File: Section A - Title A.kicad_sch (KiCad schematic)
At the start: 41 parts, among them U1 AD7190WBRUZ, Y1 ABC2-4.9152MHZ-4-T

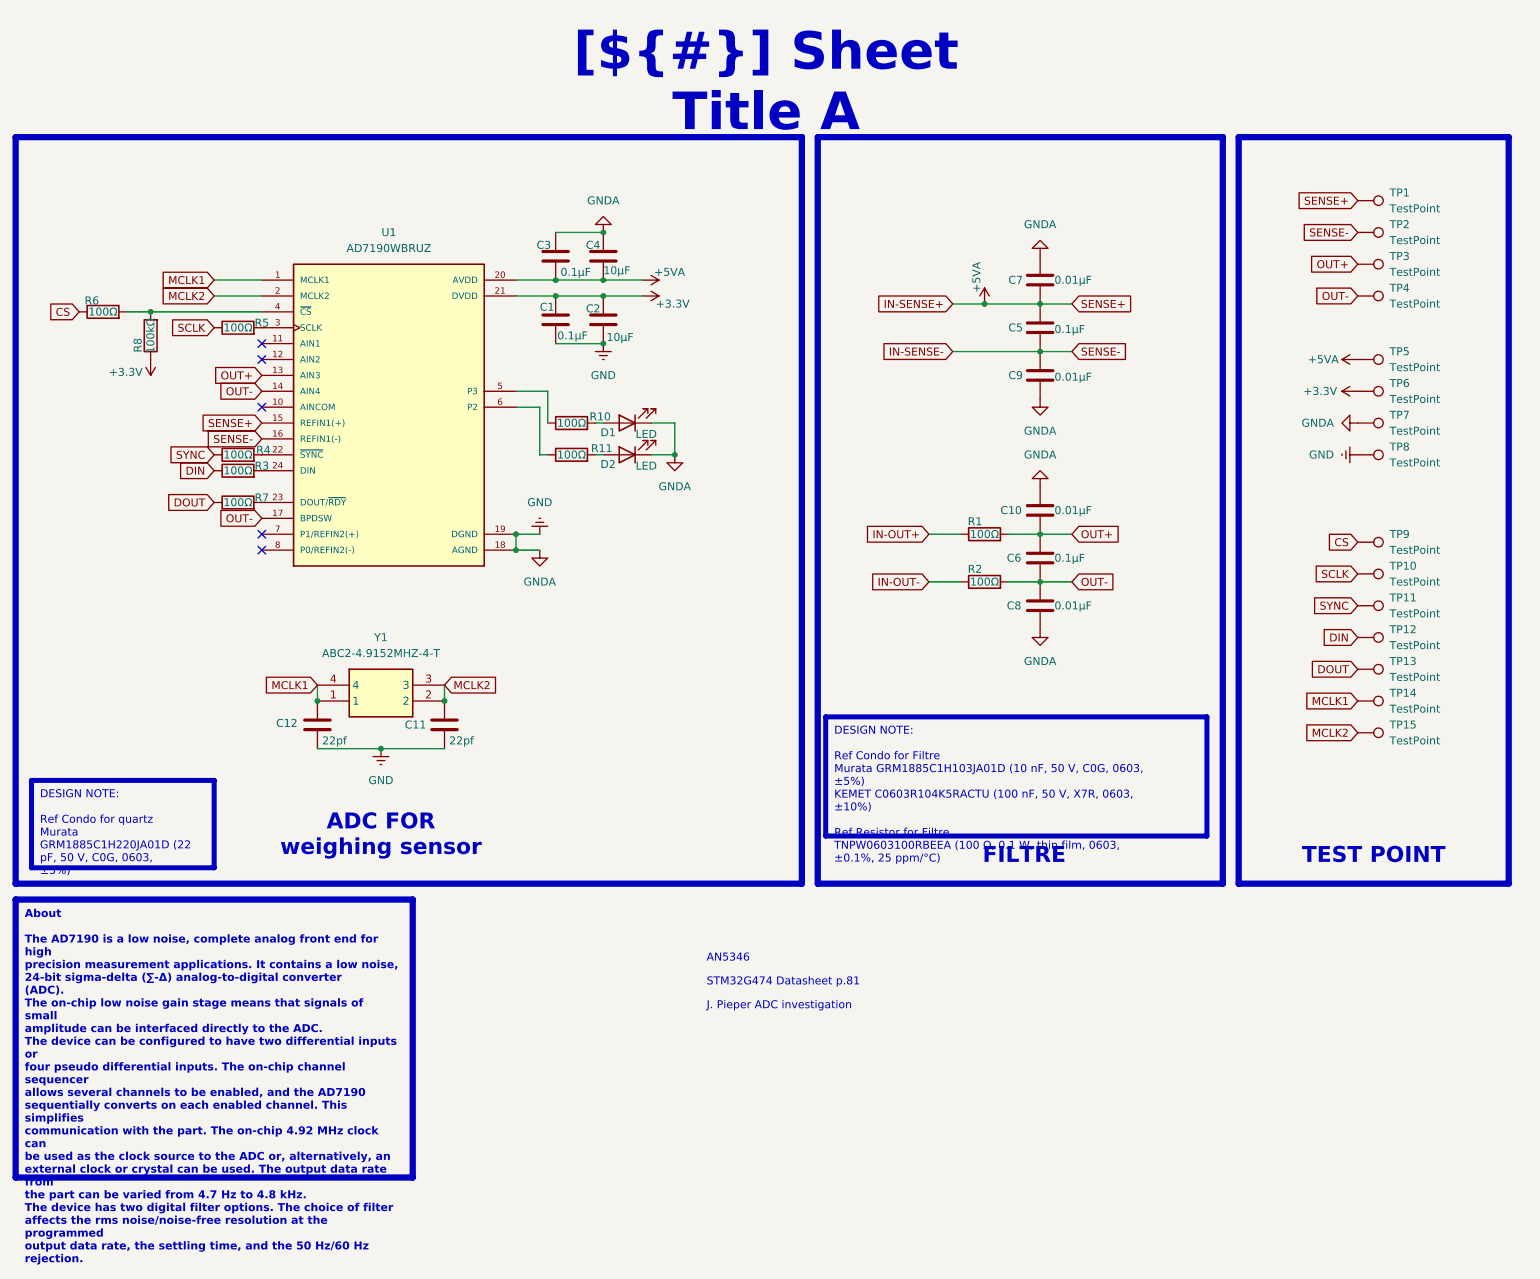
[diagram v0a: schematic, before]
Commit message: [FINISH LT3042 and ad TPS6108]
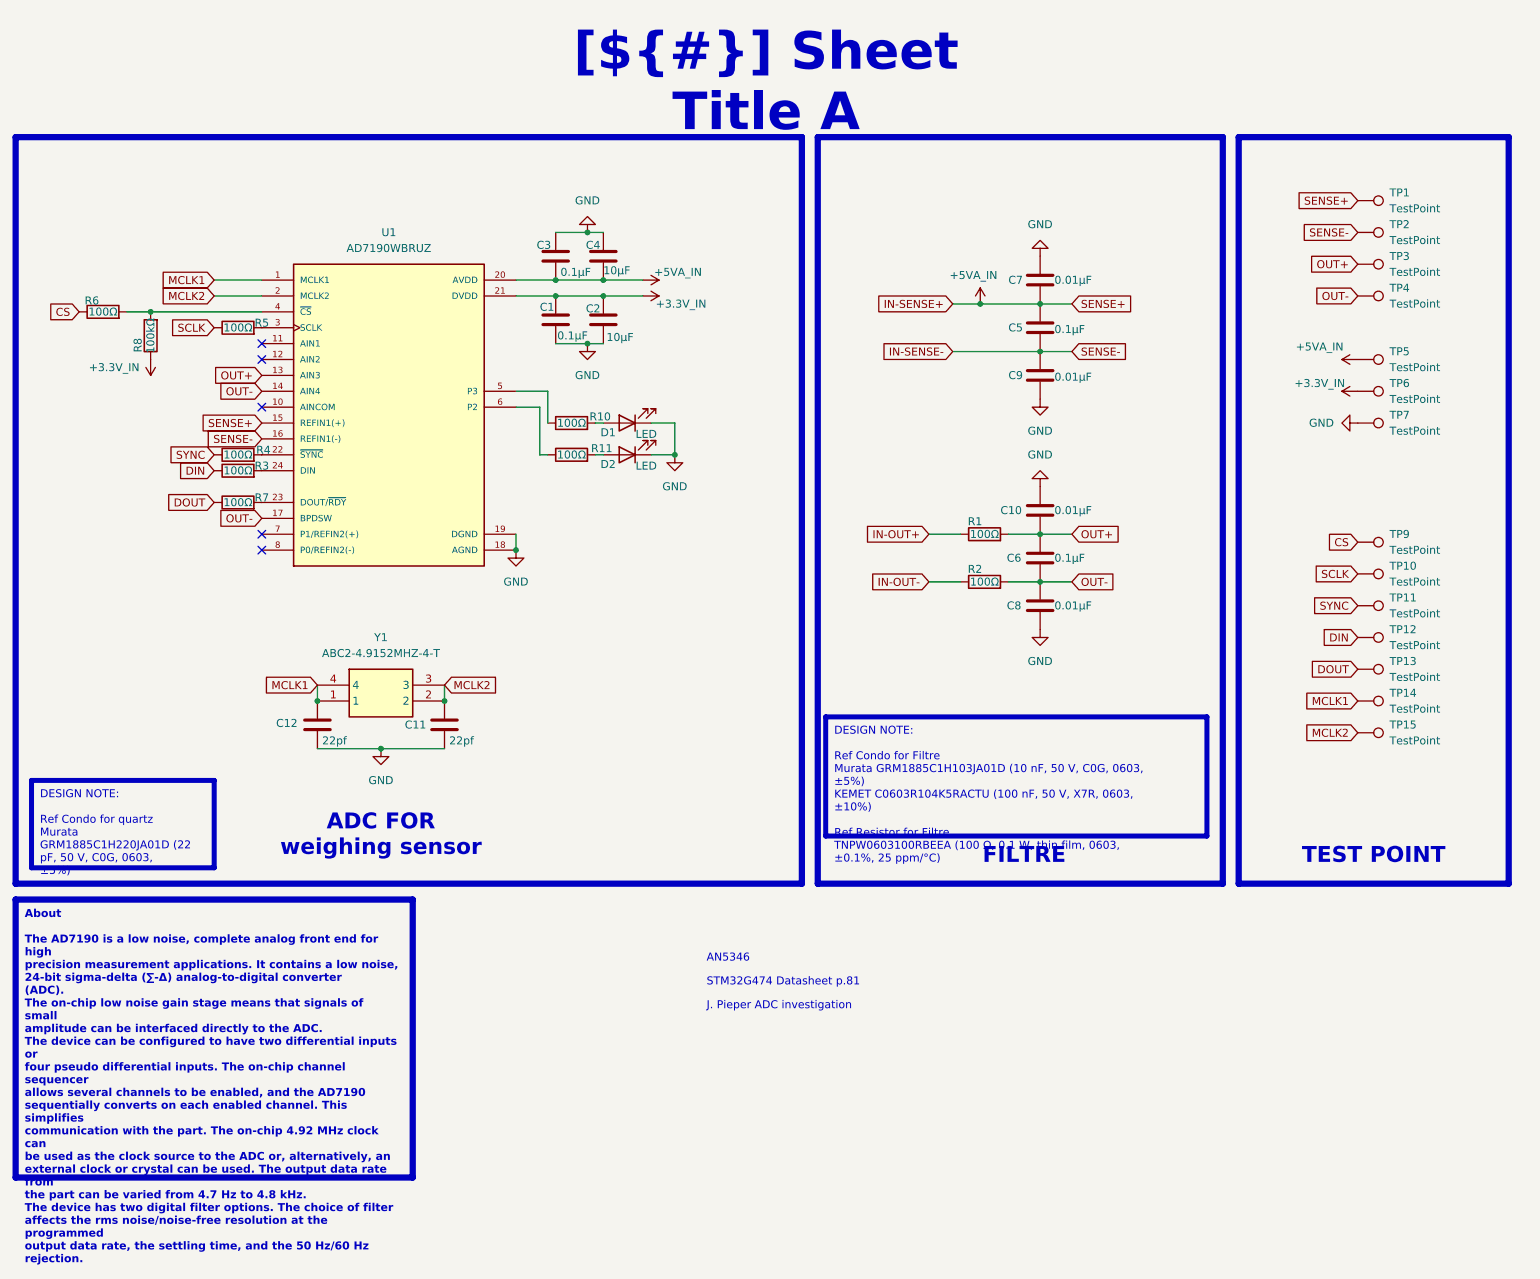
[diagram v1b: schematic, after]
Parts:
- removed TP8: TestPoint, TestPoint:TestPoint_Pad_D2.0mm, symbol Connector:TestPoint
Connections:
- net +3.3V renamed +3.3V_IN
- net +5VA renamed +5VA_IN

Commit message: [Finish schématiq]
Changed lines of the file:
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@@
 		)
 	)
-	(text_box "[${#}] ${TITLE}"
+	(text_box "[${#}] AD7910_Weight_sensor"
 		(exclude_from_sim no)
-		(at 115.57 15.24 0)
-		(size 72.39 12.7)
+		(at 92.71 15.24 0)
+		(size 113.03 12.7)
 		(margins 4.4999 4.4999 4.4999 4.4999)
 		(stroke
 			(width -0.0001)
-			(type default)
+			(type solid)
 		)
 		(fill

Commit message: [PCB fini]
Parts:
- removed TP10, TP11, TP12, TP13, TP9: TestPoint, TestPoint:TestPoint_Pad_D2.0mm, symbol Connector:TestPoint
- Y1: footprint ABC210000MHZ4 -> ABC2-4.9152MHZ-4-T:ABC210000MHZ4
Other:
- moved on the sheet: TP14, TP15

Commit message: [PCB 4 layer]
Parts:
- removed D1: LED, LED_SMD:LED_0603_1608Metric, symbol Device:LED
- removed R3, R4, R5, R7: 100Ω, Resistor_SMD:R_0603_1608Metric, symbol Device:R
- removed Y1: ABC2-4.9152MHZ-4-T, ABC2-4.9152MHZ-4-T:ABC210000MHZ4, symbol ABC2-4_9152MHZ-4-T:ABC2-4.9152MHZ-4-T
- added C23, C26: 0.1µF, Capacitor_SMD:C_0603_1608Metric, symbol Device:C
- added C24, C25: 18pf, Capacitor_SMD:C_0603_1608Metric, symbol Device:C
- added Q1: SI2303CDS-T1-GE3, Package_TO_SOT_SMD:SOT-23-3, symbol Transistor_FET:CSD25480F3
- added RN1: RP_100Ω, Resistor_SMD:R_Array_Concave_4x0603, symbol Device:R_Pack04
- added Y2: CSTCR4M91G53-R0, CSTCR4M91G53-R0:OSC_CSTCR4M91G53-R0, symbol CSTCR4M91G53-R0:CSTCR4M91G53-R0
- C11: value 22pf -> 0.1µF
- C12: value 22pf -> 10µF
- D2: value LED -> RED
- R10: value 100Ω -> 1kΩ
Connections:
- net DIN: now also RN1.5 (R4.2)
- net DOUT: now also RN1.6 (R3.2)
- net GND: now also U1.9 (NC), C23.2, C24.2, C25.2, C26.2, Y2.2
- net MCLK1: now also C25.1, Y2.1; no longer C12.1
- net MCLK2: now also C24.1, Y2.3; no longer C11.1
- net SCLK: now also RN1.8 (R1.2)
- net SYNC: now also RN1.7 (R2.2)
- net at U1.3 (SCLK): now also RN1.1 (R1.1)
- net P3: now reaches R10.1, U1.5 (P3)
- net at R10.2: now also Q1.1 (G)
- net at U1.24 (DIN): now also RN1.4 (R4.1)
- net at U1.22 (~{SYNC}): now also RN1.2 (R2.1)
- net at U1.23 (DOUT/~{RDY}): now also RN1.3 (R3.1)
- net +3.3V_IN renamed +3.3V
- net +5VA_IN renamed +5VA
- net +5VA: now also C12.1, C26.1, Q1.2 (S); no longer C5.1, C7.2, TP1.1, U1.15 (REFIN1(+))
- net IN-SENSE- renamed SENSE-
- new net SENSE+: C11.1, C23.1, C5.1, C7.2, Q1.3 (D), TP1.1, U1.15 (REFIN1(+))
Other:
- moved on the sheet: C1, C2, C3, C4, D2, R1, R11, R2, R6, R8, TP1, TP14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

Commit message: [PCB V1]
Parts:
- removed TP14, TP15: TestPoint, TestPoint:TestPoint_Pad_D2.0mm, symbol Connector:TestPoint
- added TP8, TP9: TestPoint, TestPoint:TestPoint_Pad_D1.5mm, symbol Connector:TestPoint
- TP1, TP2, TP3, TP4, TP5, TP6, TP7: footprint TestPoint:TestPoint_Pad_D2.0mm -> TestPoint:TestPoint_Pad_D1.5mm
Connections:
- net +3.3V: now also TP4.1; no longer TP6.1
- net GND: now also TP3.1; no longer TP7.1
- net MCLK1: now also TP2.1
- net MCLK2: now also TP1.1
- net OUT+: now also TP7.1; no longer TP3.1
- net OUT-: now also TP6.1; no longer TP4.1
- net SENSE+: now also TP9.1; no longer TP1.1
- net SENSE-: now also TP8.1; no longer TP2.1

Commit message: [PCB V2]
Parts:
- added TP18: TestPoint, TestPoint:TestPoint_Pad_D1.5mm, symbol Connector:TestPoint
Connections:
- net P3: now also TP18.1
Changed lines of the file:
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@@
+		)
+	)
+	(global_label "P3"
+		(shape input)
+		(at 250.19 88.9 180)
+		(fields_autoplaced yes)
+		(effects
+			(font
+				(size 1.27 1.27)
+			)
+			(justify right)
+		)
+		(property "Intersheetrefs" "${INTERSHEET_REFS}"
+			(at 244.7253 88.9 0)
+			(effects
+				(font
+					(size 1.27 1.27)
+				)
+				(justify right)
+				(hide yes)
+			)
 		)
 	)
@@
 					(unit 1)
 				)
+			)
+		)
+	)
+	(symbol
+		(lib_id "Connector:TestPoint")
+		(at 250.19 88.9 270)
+		(unit 1)
+		(exclude_from_sim no)
+		(in_bom yes)
+		(on_board yes)
+		(dnp no)
+		(fields_autoplaced yes)
+		(property "Reference" "TP18"
+			(at 255.27 87.6299 90)
+			(effects
+				(font
+					(size 1.27 1.27)
+				)
+				(justify left)
+				(hide yes)
+			)
+		)
+		(property "Value" "TestPoint"
+			(at 255.27 90.1699 90)
+			(effects
+				(font
+					(size 1.27 1.27)
+				)
+				(justify left)
+				(hide yes)
+			)
+		)
+		(property "Footprint" "TestPoint:TestPoint_Pad_D1.5mm"
+			(at 250.19 93.98 0)
+			(effects
+				(font
+					(size 1.27 1.27)
+				)
+				(hide yes)
+			)
+		)
+		(property "Datasheet" "~"
+			(at 250.19 93.98 0)
+			(effects
+				(font
+					(size 1.27 1.27)
+				)
+				(hide yes)
+			)
+		)
+		(property "Description" "test point"
+			(at 250.19 88.9 0)
+			(effects
+				(font
+					(size 1.27 1.27)
+				)
+				(hide yes)
+			)
+		)
+		(pin "1"
+		)
+		(instances
+			(project "Cellule_de_force_V2"
+				(path "/f9e05184-c88b-4a88-ae9c-ab2bdb32be7c/c5103ceb-5325-4a84-a025-9638a412984e/f06537ee-772d-44d3-8c50-e0ba41038c9c"
+					(reference "TP18")
+					(unit 1)
+				)

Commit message: [PCB V3]
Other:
- moved on the sheet: C24, C25, D2, Y2
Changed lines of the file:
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@@
 	)
 	(junction
-		(at 100.33 125.73)
+		(at 99.06 125.73)
 		(diameter 0)
 		(color 0 0 0 0)
@@
 	)
 	(junction
-		(at 113.03 113.03)
+		(at 111.76 113.03)
 		(diameter 0)
 		(color 0 0 0 0)
@@
 	)
 	(junction
-		(at 87.63 113.03)
+		(at 86.36 113.03)
 		(diameter 0)
 		(color 0 0 0 0)
@@
 	(wire
 		(pts
-			(xy 119.38 113.03) (xy 113.03 113.03)
+			(xy 114.3 113.03) (xy 111.76 113.03)
 		)
 		(stroke
@@
 	(wire
 		(pts
-			(xy 113.03 125.73) (xy 100.33 125.73)
+			(xy 111.76 125.73) (xy 99.06 125.73)
 		)
 		(stroke
@@
 	(wire
 		(pts
-			(xy 113.03 120.65) (xy 113.03 125.73)
+			(xy 111.76 120.65) (xy 111.76 125.73)
 		)
 		(stroke
@@
 	(wire
 		(pts
-			(xy 87.63 120.65) (xy 87.63 125.73)
+			(xy 86.36 120.65) (xy 86.36 125.73)
 		)
 		(stroke
@@
 	(wire
 		(pts
-			(xy 130.81 72.39) (xy 133.35 72.39)
+			(xy 130.81 72.39) (xy 132.08 72.39)
 		)
 		(stroke
@@
 	(wire
 		(pts
-			(xy 83.82 113.03) (xy 87.63 113.03)
+			(xy 82.55 113.03) (xy 86.36 113.03)
 		)
 		(stroke
@@
 	(wire
 		(pts
-			(xy 140.97 72.39) (xy 146.05 72.39)
+			(xy 139.7 72.39) (xy 146.05 72.39)
 		)
 		(stroke
@@
 	(wire
 		(pts
-			(xy 87.63 125.73) (xy 100.33 125.73)
+			(xy 86.36 125.73) (xy 99.06 125.73)
 		)
 		(stroke
@@
 	(global_label "MCLK1"
 		(shape input)
-		(at 83.82 113.03 180)
+		(at 82.55 113.03 180)
 		(fields_autoplaced yes)
 		(effects
@@
 		)
 		(property "Intersheetrefs" "${INTERSHEET_REFS}"
-			(at 74.6058 113.03 0)
+			(at 73.3358 113.03 0)
 			(effects
 				(font
@@
 	(global_label "MCLK2"
 		(shape input)
-		(at 119.38 113.03 0)
+		(at 114.3 113.03 0)
 		(fields_autoplaced yes)
 		(effects
@@
 		)
 		(property "Intersheetrefs" "${INTERSHEET_REFS}"
-			(at 128.5942 113.03 0)
+			(at 123.5142 113.03 0)
 			(effects
 				(font
@@
 	(symbol
 		(lib_id "Device:C")
-		(at 113.03 116.84 0)
+		(at 111.76 116.84 0)
 		(unit 1)
 		(exclude_from_sim no)
@@
 		(dnp no)
 		(property "Reference" "C24"
-			(at 113.284 118.872 0)
+			(at 112.014 118.872 0)
 			(effects
 				(font
@@
 		)
 		(property "Value" "18pf"
-			(at 115.57 116.84 0)
+			(at 114.3 116.84 0)
 			(effects
 				(font
@@
 		)
 		(property "Footprint" "Capacitor_SMD:C_0603_1608Metric"
-			(at 113.9952 120.65 0)
+			(at 112.7252 120.65 0)
 			(effects
 				(font
@@
 		)
 		(property "Datasheet" "~"
-			(at 113.03 116.84 0)
+			(at 111.76 116.84 0)
 			(effects
 				(font
@@
 		)
 		(property "Description" "Unpolarized capacitor"
-			(at 113.03 116.84 0)
+			(at 111.76 116.84 0)
 			(effects
 				(font
@@
 	(symbol
 		(lib_id "CSTCR4M91G53-R0:CSTCR4M91G53-R0")
-		(at 100.33 115.57 0)
+		(at 99.06 115.57 0)
 		(unit 1)
 		(exclude_from_sim no)
@@
 		(fields_autoplaced yes)
 		(property "Reference" "Y2"
-			(at 100.33 105.41 0)
+			(at 99.06 105.41 0)
 			(effects
 				(font
@@
 		)
 		(property "Value" "CSTCR4M91G53-R0"
-			(at 100.33 107.95 0)
+			(at 99.06 107.95 0)
 			(effects
 				(font
@@
 		)
 		(property "Footprint" "CSTCR4M91G53-R0:OSC_CSTCR4M91G53-R0"
-			(at 100.33 115.57 0)
+			(at 99.06 115.57 0)
 			(effects
 				(font
@@
 		)
 		(property "Datasheet" ""
-			(at 100.33 115.57 0)
+			(at 99.06 115.57 0)
 			(effects
 				(font
@@
 		)
 		(property "Description" ""
-			(at 100.33 115.57 0)
+			(at 99.06 115.57 0)
 			(effects
 				(font
@@
 		)
 		(property "MF" "Murata Electronics"
-			(at 100.33 115.57 0)
+			(at 99.06 115.57 0)
 			(effects
 				(font
@@
 		)
 		(property "MAXIMUM_PACKAGE_HEIGHT" "1.2mm"
-			(at 100.33 115.57 0)
+			(at 99.06 115.57 0)
 			(effects
 				(font
@@
 		)
 		(property "Package" "SMD-3 Murata"
-			(at 100.33 115.57 0)
+			(at 99.06 115.57 0)
 			(effects
 				(font
@@
 		)
 		(property "Price" "None"
-			(at 100.33 115.57 0)
+			(at 99.06 115.57 0)
 			(effects
 				(font
@@
 		)
 		(property "Check_prices" "https://www.snapeda.com/parts/CSTCR4M91G53-R0/Murata+Electronics+North+America/view-part/?ref=eda"
-			(at 100.33 115.57 0)
+			(at 99.06 115.57 0)
 			(effects
 				(font
@@
 		)
 		(property "STANDARD" "Manufacturer Recomendations"
-			(at 100.33 115.57 0)
+			(at 99.06 115.57 0)
 			(effects
 				(font
@@
 		)
 		(property "PARTREV" "JGC42-8797"
-			(at 100.33 115.57 0)
+			(at 99.06 115.57 0)
 			(effects
 				(font
@@
 		)
 		(property "SnapEDA_Link" "https://www.snapeda.com/parts/CSTCR4M91G53-R0/Murata+Electronics+North+America/view-part/?ref=snap"
-			(at 100.33 115.57 0)
+			(at 99.06 115.57 0)
 			(effects
 				(font
@@
 		)
 		(property "MP" "CSTCR4M91G53-R0"
-			(at 100.33 115.57 0)
+			(at 99.06 115.57 0)
 			(effects
 				(font
@@
 		)
 		(property "Purchase-URL" "https://www.snapeda.com/api/url_track_click_mouser/?unipart_id=50325&manufacturer=Murata Electronics&part_name=CSTCR4M91G53-R0&search_term=cstcr4m91g53-r0"
-			(at 100.33 115.57 0)
+			(at 99.06 115.57 0)
 			(effects
 				(font
@@
 		)
 		(property "Description_1" "4.91 MHz Ceramic Resonator Built in Capacitor 15 pF ±0.2% 60 Ohms -20°C ~ 80°C Surface Mount"
-			(at 100.33 115.57 0)
+			(at 99.06 115.57 0)
 			(effects
 				(font
@@
 		)
 		(property "Availability" "In Stock"
-			(at 100.33 115.57 0)
+			(at 99.06 115.57 0)
 			(effects
 				(font
@@
 		)
 		(property "MANUFACTURER" "Murata"
-			(at 100.33 115.57 0)
+			(at 99.06 115.57 0)
 			(effects
 				(font
@@
 	(symbol
 		(lib_id "power:GND")
-		(at 100.33 125.73 0)
+		(at 99.06 125.73 0)
 		(unit 1)
 		(exclude_from_sim no)
@@
 		(fields_autoplaced yes)
 		(property "Reference" "#PWR013"
-			(at 100.33 132.08 0)
+			(at 99.06 132.08 0)
 			(effects
 				(font
@@
 		)
 		(property "Value" "GND"
-			(at 100.33 130.81 0)
+			(at 99.06 130.81 0)
 			(effects
 				(font
@@
 		)
 		(property "Footprint" ""
-			(at 100.33 125.73 0)
+			(at 99.06 125.73 0)
 			(effects
 				(font
@@
 		)
 		(property "Datasheet" ""
-			(at 100.33 125.73 0)
+			(at 99.06 125.73 0)
 			(effects
 				(font
@@
 		)
 		(property "Description" "Power symbol creates a global label with name \"GND\" , ground"
-			(at 100.33 125.73 0)
+			(at 99.06 125.73 0)
 			(effects
 				(font
@@
 	(symbol
 		(lib_id "Device:C")
-		(at 87.63 116.84 0)
+		(at 86.36 116.84 0)
 		(unit 1)
 		(exclude_from_sim no)
@@
 		(dnp no)
 		(property "Reference" "C25"
-			(at 83.312 119.126 0)
+			(at 82.042 119.126 0)
 			(effects
 				(font
@@
 		)
 		(property "Value" "18pf"
-			(at 81.28 116.586 0)
+			(at 80.01 116.586 0)
 			(effects
 				(font
@@
 		)
 		(property "Footprint" "Capacitor_SMD:C_0603_1608Metric"
-			(at 88.5952 120.65 0)
+			(at 87.3252 120.65 0)
 			(effects
 				(font
@@
 		)
 		(property "Datasheet" "~"
-			(at 87.63 116.84 0)
+			(at 86.36 116.84 0)
 			(effects
 				(font
@@
 		)
 		(property "Description" "Unpolarized capacitor"
-			(at 87.63 116.84 0)
+			(at 86.36 116.84 0)
 			(effects
 				(font
@@
 	(symbol
 		(lib_id "Device:LED")
-		(at 137.16 72.39 180)
+		(at 135.89 72.39 180)
 		(unit 1)
 		(exclude_from_sim no)
@@
 		(dnp no)
 		(property "Reference" "D2"
-			(at 134.112 70.612 0)
+			(at 132.842 70.612 0)
 			(effects
 				(font
@@
 		)
 		(property "Value" "RED"
-			(at 137.414 74.93 0)
+			(at 136.144 74.93 0)
 			(effects
 				(font
@@
 		)
 		(property "Footprint" "LED_SMD:LED_0603_1608Metric"
-			(at 137.16 72.39 0)
+			(at 135.89 72.39 0)
 			(effects
 				(font
@@
 		)
 		(property "Datasheet" "~"
-			(at 137.16 72.39 0)
+			(at 135.89 72.39 0)
 			(effects
 				(font
@@
 		)
 		(property "Description" "Light emitting diode"
-			(at 137.16 72.39 0)
+			(at 135.89 72.39 0)
 			(effects
 				(font
@@
 		)
 		(property "Sim.Pins" "1=K 2=A"
-			(at 137.16 72.39 0)
+			(at 135.89 72.39 0)
 			(effects
 				(font

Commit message: [PCB V4]
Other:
- note added: "AD7190"
- note added: "AD7190_TEST_BOARD CN"
- note added: "CSTCR4M91G53-R0"
- note removed: "AN5346"
- note removed: "J. Pieper ADC investigation"
- note removed: "STM32G474 Datasheet p.81"
